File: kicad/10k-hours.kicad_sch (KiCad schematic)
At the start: 32 parts, among them P1 USB_C_Plug_USB2.0, Q1 PMOS, SW1 SW_Push, U1 TM1637, U2 STM32C011F6Px, U3 TODO-, U5 MCP73831, U6 PAM2306AYPKE, U7 DW01, U8 FH8205A

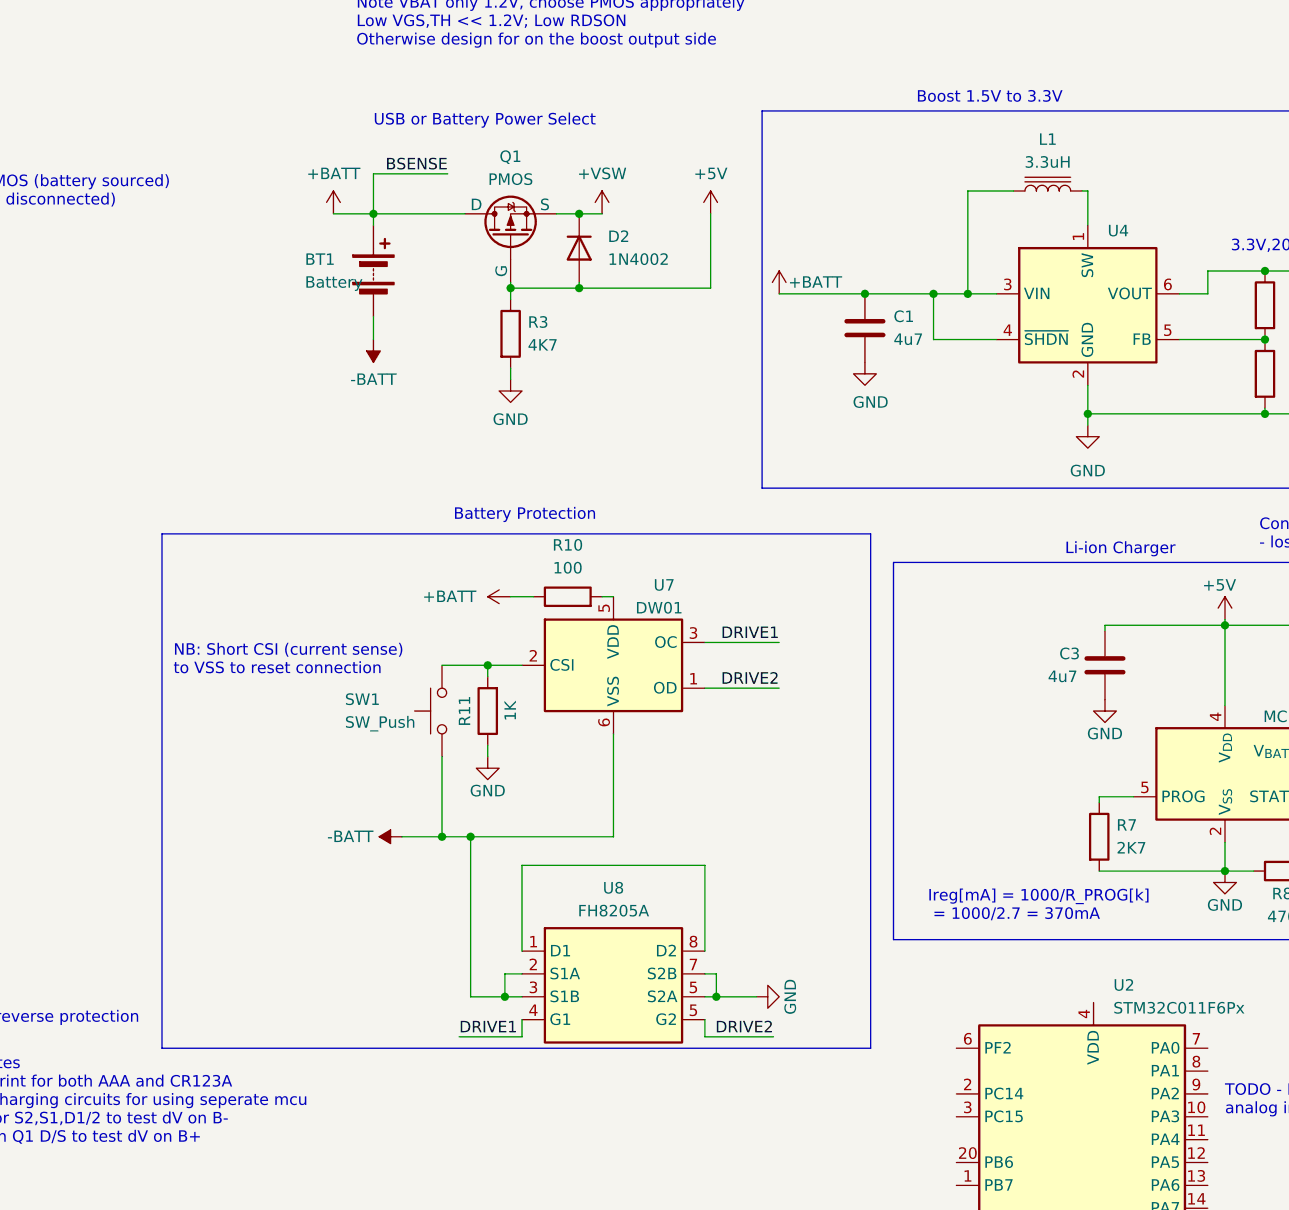
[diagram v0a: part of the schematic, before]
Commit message: protection circuit
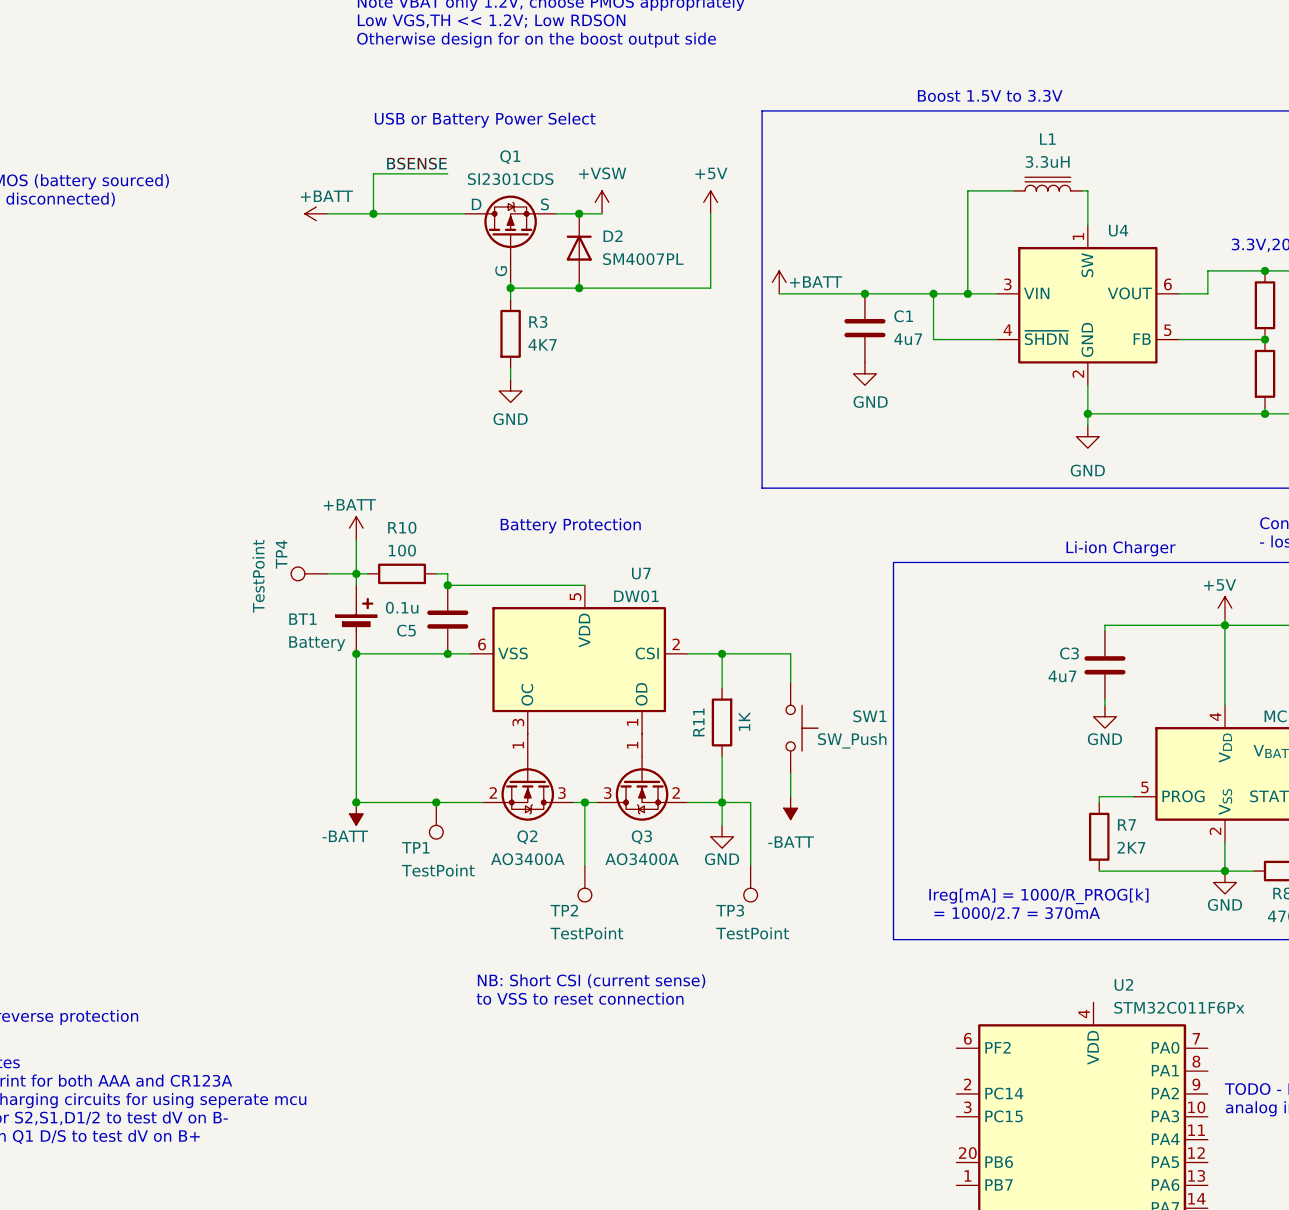
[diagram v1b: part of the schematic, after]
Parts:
- removed BT1: Battery, symbol Device:Battery
- removed U8: FH8205A, Package_SO:HTSOP-8-1EP_3.9x4.9mm_P1.27mm_EP2.4x3.2mm, symbol User_10K-Hours:FS8205
- added BT1: Battery, symbol Device:Battery_Cell
- added C5: 0.1u, symbol Device:C
- added Q2, Q3: AO3400A, Package_TO_SOT_SMD:SOT-23, symbol Transistor_FET:AO3400A
- added TP1, TP2, TP4: TestPoint, symbol Connector:TestPoint
- added TP3: TestPoint, TestPoint:TestPoint_Pad_D2.0mm, symbol Connector:TestPoint
- D2: value 1N4002 -> SM4007PL; JLCPCB PN (none) -> C64898; MPN (none) -> SM4007PL; Manufacturer (none) -> MDD(Microdiode Semiconductor)
- Q1: value PMOS -> SI2301CDS; JLCPCB PN (none) -> C10487; MPN (none) -> SI2301CDS-T1-GE3; Manufacturer (none) -> Vishay Intertech
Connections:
- net +BATT: now also BT1.1 (+), TP4.1
- net -BATT: now also BT1.2 (-), C5.2, Q2.2 (S), TP1.1
- net GND: now also Q3.2 (S), TP3.1
- net at R10.2, U7.5 (VDD): now also C5.1
- net DRIVE1: no longer names the net of U7.3 (OC)
- net DRIVE1: now also Q2.1 (G)
- net DRIVE2: no longer names the net of U7.1 (OD)
- net DRIVE2: now also Q3.1 (G)
- new net: Q2.3 (D), Q3.3 (D), TP2.1
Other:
- moved on the sheet: R10, U7

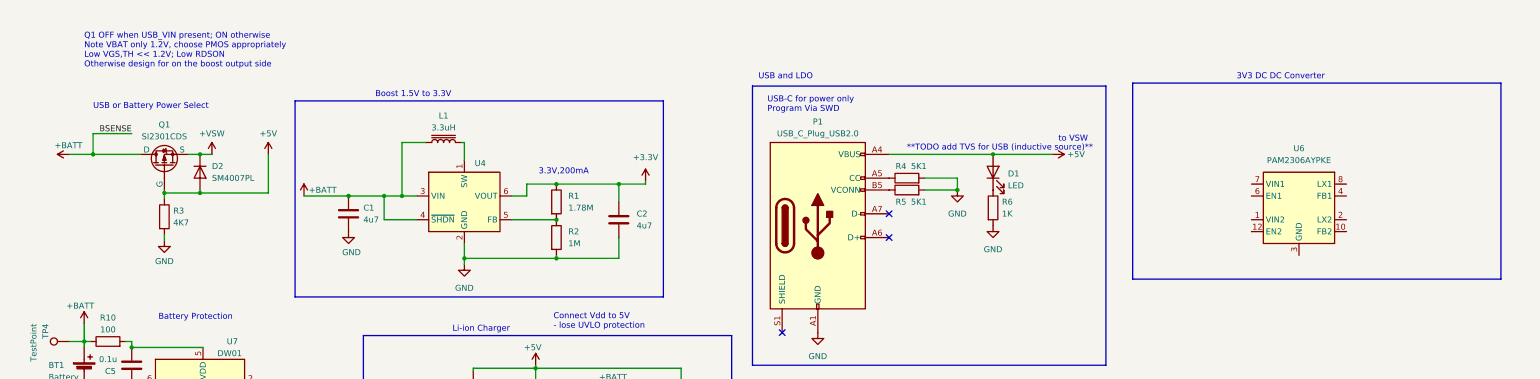
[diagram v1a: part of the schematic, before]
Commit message: dc dc converter and cap selection
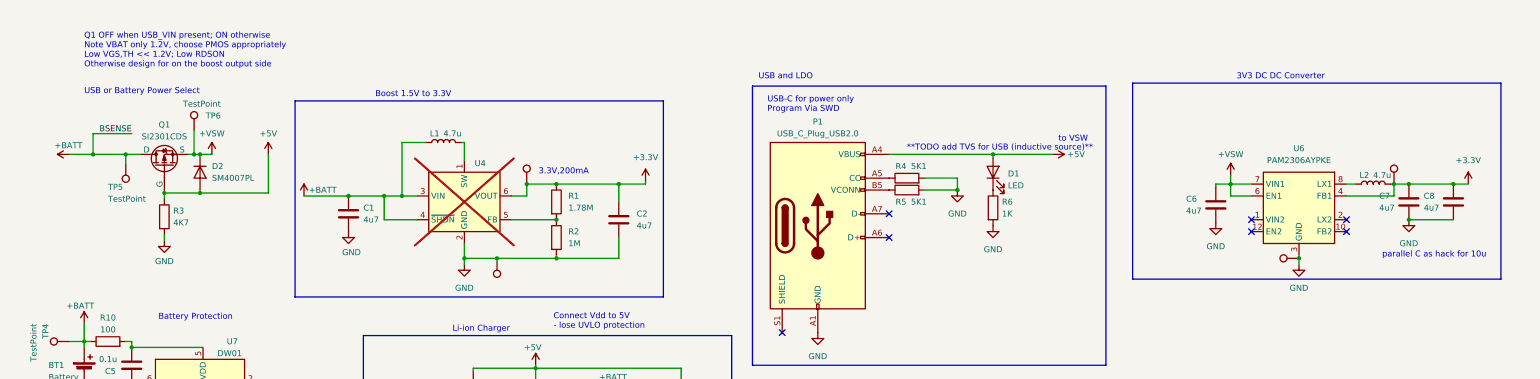
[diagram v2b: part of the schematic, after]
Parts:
- removed L1: 3.3uH, symbol Device:L_Iron
- added C6, C7, C8: 4u7, symbol Device:C
- added L1, L2: 4.7u, symbol Device:L
- added TP10, TP5, TP6, TP7, TP8, TP9: TestPoint, TestPoint:TestPoint_Pad_D2.0mm, symbol Connector:TestPoint
- C1, C2, C3, C4: JLCPCB PN (none) -> C19666; MPN (none) -> CL10A475KO8NNNC; Manufacturer (none) -> Samsung Electro-Mechanics
- C5: JLCPCB PN (none) -> C1525; MPN (none) -> CL05B104KO5NNNC; Manufacturer (none) -> Samsung Electro-Mechanics
- U4: now not fitted
- U6: footprint Package_DFN_QFN:WDFN-12-1EP_3x3mm_P0.45mm_EP1.7x2.5mm -> TODO
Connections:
- net +3.3V: now also U6.4 (FB1), C7.1, C8.1, L2.2, TP10.1, TP8.1
- net +BATT: now also L1.1, TP5.1
- net +VSW: now also U6.6 (EN1), U6.7 (VIN1), C6.1, TP6.1
- net GND: now also U6.13 (GND), U6.3 (GND), U6.9 (GND), C6.2, C7.2, C8.2, TP7.1, TP9.1
- net at U6.8 (LX1): now also L2.1
- net at U4.1 (SW): now also L1.2
- no-connect marks 3 -> 7
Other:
- note added: "parallel C as hack for 10u"

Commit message: user io start
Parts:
- added C9: 0.1u, symbol Device:C
- added R12, R14: 100, symbol Device:R
- added R13: 10k, symbol Device:R
- added SW3, SW4: SW_Push, symbol Switch:SW_Push
- added U8: TODO-, Display_7Segment:CA56-12CGKWA, symbol Display_Character:CA56-12CGKWA
- U2: value STM32C011F6Px -> STM32C011F6P6; JLCPCB PN (none) -> C5456198
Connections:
- net +3.3V: now also SW3.1
- net GND: now also C9.2, R13.2, SW4.1
- net SWDIO: now reaches U2.18 (PA13)
- net SWCLK_BOOT0: now reaches U2.19 (PA14)
- net OSCX_IN: now reaches U2.2 (PC14)
- net OSCX_OUT: now reaches U2.3 (PC15)
- new net: R12.2, SW3.2
- new net: R14.2, SW4.2
- new net IN2: R14.1
- new net WAKE_IN1: C9.1, R12.1, R13.1
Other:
- note added: "GPIO"
- note added: "Internal Pullup"
- note added: "STM32duino supports C0F6 as of 2.6.0"
- note removed: "TODO - Low voltage indicator analog input"
- moved on the sheet: BT1, C1, C2, C3, C4, C5, C6, C7, C8, D1, D2, D3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

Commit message: usb uart start
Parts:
- added C10, C11: 0.1uF, symbol Device:C
- added U9: CH340C, Package_SO:SOIC-16_3.9x9.9mm_P1.27mm, symbol Interface_USB:CH340C
- C1, C2, C3, C4, C6, C7, C8: value 4u7 -> 4u7F
- C5, C9: value 0.1u -> 0.1uF
- L1, L2: value 4.7u -> 4.7uH
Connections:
- net +5V: now also C10.1, U9.4 (V3)
- net GND: now also C10.2, C11.1
- net USB_D+: now reaches P1.A6 (D+)
- net USB_D+: now also U9.5 (UD+)
- net USB_D-: now reaches P1.A7 (D-)
- net USB_D-: now also U9.6 (UD-)
- new net: C11.2, U9.16 (VCC)
- new net PROG_RX: U9.2 (TXD)
- new net PROG_TX: U9.3 (RXD)
- new net ~{DTR}: U9.13 (~{DTR})
- new net ~{RTS}: U9.14 (~{RTS})
- no-connect marks 7 -> 9
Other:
- moved on the sheet: C6, C7, C8, L2, U1, U3, U6, U8

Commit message: edits
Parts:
- removed U9: CH340C, Package_SO:SOIC-16_3.9x9.9mm_P1.27mm, symbol Interface_USB:CH340C
- added J1: Conn_01x06_Pin, symbol Connector:Conn_01x06_Pin
- added Q4, Q5, Q6: AO3400A, Package_TO_SOT_SMD:SOT-23, symbol Transistor_FET:AO3400A
- added R15, R16, R17: 4K7, symbol Device:R
- added R18, R19: 10K, symbol Device:R
- C10, C11: value 0.1uF -> 100nF; JLCPCB PN C1525 -> C19666; MPN CL05B104KO5NNNC -> CL10A475KO8NNNC
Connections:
- net +3.3V: now also C10.1, J1.1 (Pin_1), R15.1, R16.1, R17.1
- net +5V: no longer C10.1
- net GND: now also J1.3 (Pin_3), Q4.2 (S), Q5.2 (S), Q6.2 (S)
- net SWCLK_BOOT0: now also J1.2 (Pin_2)
- net SWDIO: now also J1.4 (Pin_4)
- net nRST: now reaches C11.2
- net nRST: now also J1.5 (Pin_5)
- new net: Q4.3 (D), R16.2, R19.1
- new net: Q5.3 (D), R15.2, R18.1
- new net: Q6.1 (G), R18.2, R19.2
- new net CC1_CON: Q5.1 (G)
- new net CC2_CON: Q4.1 (G)
- new net DAM_Active: Q6.3 (D), R17.2
- new net SWO: J1.6 (Pin_6)
- no-connect marks 9 -> 5
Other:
- note added: "For DAM if both CC1 and CC2 are pulled high by host, we switch the MUX for the SWD pins"
- note added: "Normally ON => 0V out"
- note added: "SWD Programmer"
- note added: "follow STLink v2 stand-alone header NB C0 does not have SWO"
- note added: "forgo TVS for cost"
- note removed: "STM32duino supports C0F6 as of 2.6.0"
